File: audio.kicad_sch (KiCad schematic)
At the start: 8 parts, among them J1 1775443-2, U11 MAX98357AETE_T

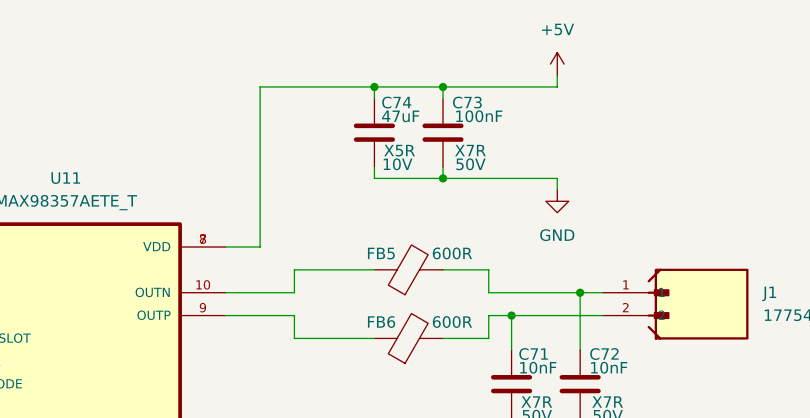
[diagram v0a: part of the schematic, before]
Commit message: modifications for manufacturing
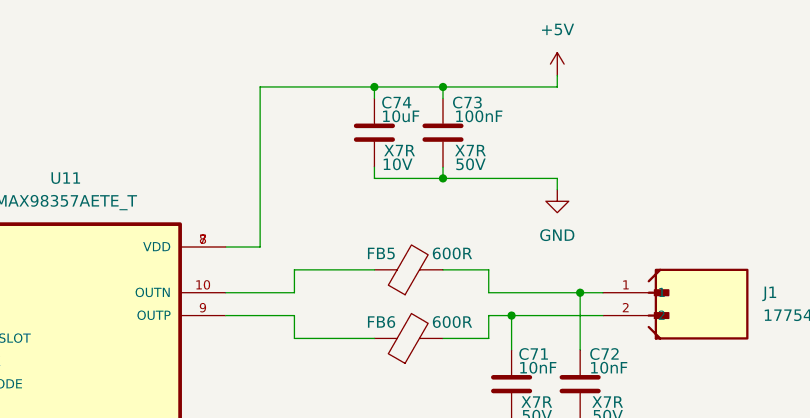
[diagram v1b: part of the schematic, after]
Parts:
- C73: Supplier Part (none) -> C49678
- C74: value 47uF -> 10uF; Dielectric X5R -> X7R; Supplier Part (none) -> C86038
- FB5, FB6: MANUFACTURER (none) -> Murata Electronics; MP (none) -> BLM18KG601SN1D; Part number BLM18AG601SN1D -> BLM18KG601SN1D; Supplier Part (none) -> C85833
- J1: Supplier Part (none) -> C5162845
- U11: Availability In Stock -> (none); Check_prices https://www.snapeda.com/parts/MAX98357AETE+T/Analog+Devices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 -> (none); Description_1 Tiny, Low-Cost, PCM Class D Amplifier with Class AB Perform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 -> (none); MANUFACTURER (none) -> Analog Devices Inc./Maxim Integrated; Package TQFN-16 Maxim -> TQFN-16-EP(3x3); Price None -> (none); Supplier Part (none) -> C910544
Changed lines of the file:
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@@
+			)
+		)
+		(property "Supplier Part" "C5162845"
+			(at 196.85 80.01 0)
+			(effects
+				(font
+					(size 1.27 1.27)
+				)
+				(hide yes)
 			)
 		)
@@
 			)
 		)
-		(property "Value" "47uF"
+		(property "Value" "10uF"
 			(at 167.132 60.452 0)
 			(effects
@@
 			)
 		)
-		(property "Dielectric" "X5R"
+		(property "Dielectric" "X7R"
 			(at 169.164 64.262 0)
 			(effects
@@
 		)
 		(property "Function" "AUDIO"
+			(at 166.37 62.23 0)
+			(effects
+				(font
+					(size 1.27 1.27)
+				)
+				(hide yes)
+			)
+		)
+		(property "Supplier Part" "C86038"
 			(at 166.37 62.23 0)
 			(effects
@@
 			)
 		)
-		(property "Part number" "BLM18AG601SN1D"
+		(property "Part number" "BLM18KG601SN1D"
 			(at 170.18 77.47 90)
 			(effects
@@
 		)
 		(property "Manufacturer" "Murata"
+			(at 170.18 77.47 90)
+			(effects
+				(font
+					(size 1.27 1.27)
+				)
+				(hide yes)
+			)
+		)
+		(property "Supplier Part" "C85833"
+			(at 170.18 77.47 90)
+			(effects
+				(font
+					(size 1.27 1.27)
+				)
+				(hide yes)
+			)
+		)
+		(property "MANUFACTURER" "Murata Electronics"
+			(at 170.18 77.47 90)
+			(effects
+				(font
+					(size 1.27 1.27)
+				)
+				(hide yes)
+			)
+		)
+		(property "MP" "BLM18KG601SN1D"
 			(at 170.18 77.47 90)
 			(effects
@@
 			)
 		)
+		(property "Supplier Part" "C49678"
+			(at 173.99 62.23 0)
+			(effects
+				(font
+					(size 1.27 1.27)
+				)
+				(hide yes)
+			)
+		)
 		(pin "1"
 		)
@@
 			)
 		)
-		(property "Part number" "BLM18AG601SN1D"
+		(property "Part number" "BLM18KG601SN1D"
 			(at 170.18 85.09 90)
 			(effects
@@
 		)
 		(property "Manufacturer" "Murata"
+			(at 170.18 85.09 90)
+			(effects
+				(font
+					(size 1.27 1.27)
+				)
+				(hide yes)
+			)
+		)
+		(property "Supplier Part" "C85833"
+			(at 170.18 85.09 90)
+			(effects
+				(font
+					(size 1.27 1.27)
+				)
+				(hide yes)
+			)
+		)
+		(property "MANUFACTURER" "Murata Electronics"
+			(at 170.18 85.09 90)
+			(effects
+				(font
+					(size 1.27 1.27)
+				)
+				(hide yes)
+			)
+		)
+		(property "MP" "BLM18KG601SN1D"
 			(at 170.18 85.09 90)
 			(effects
@@
 			)
 		)
-		(property "Description" ""
+		(property "Description" "Monaural 3.2Wx2@4Ω TQFN-16-EP(3x3) Audio Amplifiers ROHS"
 			(at 132.08 87.63 0)
 			(effects
@@
 			)
 		)
-		(property "Description_1" "Tiny, Low-Cost, PCM Class D Amplifier with Class AB Performance"
+		(property "Package" "TQFN-16-EP(3x3)"
 			(at 132.08 87.63 0)
 			(effects
@@
 			)
 		)
-		(property "Package" "TQFN-16 Maxim"
+		(property "SnapEDA_Link" "https://www.snapeda.com/parts/MAX98357AETE+T/Analog+Devices/view-part/?ref=snap"
 			(at 132.08 87.63 0)
 			(effects
@@
 			)
 		)
-		(property "Price" "None"
+		(property "MP" "MAX98357AETE+T"
 			(at 132.08 87.63 0)
 			(effects
@@
 			)
 		)
-		(property "SnapEDA_Link" "https://www.snapeda.com/parts/MAX98357AETE+T/Analog+Devices/view-part/?ref=snap"
-			(at 132.08 87.63 0)
-			(effects
-				(font
-					(size 1.27 1.27)
-				)
-				(justify bottom)
-				(hide yes)
-			)
-		)
-		(property "MP" "MAX98357AETE+T"
-			(at 132.08 87.63 0)
-			(effects
-				(font
-					(size 1.27 1.27)
-				)
-				(justify bottom)
-				(hide yes)
-			)
-		)
-		(property "Availability" "In Stock"
-			(at 132.08 87.63 0)
-			(effects
-				(font
-					(size 1.27 1.27)
-				)
-				(justify bottom)
-				(hide yes)
-			)
-		)
-		(property "Check_prices" "https://www.snapeda.com/parts/MAX98357AETE+T/Analog+Devices/view-part/?ref=eda"
-			(at 132.08 87.63 0)
-			(effects
-				(font
-					(size 1.27 1.27)
-				)
-				(justify bottom)
-				(hide yes)
-			)
-		)
 		(property "Function" "AUDIO"
 			(at 132.08 87.63 0)
 			(effects
+				(font
+					(size 1.27 1.27)
+				)
+				(hide yes)
+			)
+		)
+		(property "Supplier Part" "C910544"
+			(at 132.08 87.63 0)
+			(effects
+				(font
+					(size 1.27 1.27)
+				)
+				(hide yes)
+			)
+		)
+		(property "MANUFACTURER" "Analog Devices Inc./Maxim Integrated"
+			(at 132.08 87.63 0)
+			(effects

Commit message: modifications for manufacturing
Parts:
- C71, C72: Supplier Part (none) -> C1710
- FB5, FB6: Manufacturer Part (none) -> BLM18KG601SN1D
- J1: Manufacturer (none) -> TE Connectivity; Manufacturer Part (none) -> 1775443-2
- U11: Manufacturer (none) -> Analog Devices Inc./Maxim Integrated; Manufacturer Part (none) -> MAX98357AETE+T
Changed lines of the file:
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@@
+			)
+		)
+		(property "Manufacturer" "TE Connectivity"
+			(at 196.85 80.01 0)
+			(effects
+				(font
+					(size 1.27 1.27)
+				)
+				(hide yes)
+			)
+		)
+		(property "Manufacturer Part" "1775443-2"
+			(at 196.85 80.01 0)
+			(effects
+				(font
+					(size 1.27 1.27)
+				)
+				(hide yes)
 			)
 		)
@@
 		)
 		(property "MP" "BLM18KG601SN1D"
+			(at 170.18 77.47 90)
+			(effects
+				(font
+					(size 1.27 1.27)
+				)
+				(hide yes)
+			)
+		)
+		(property "Manufacturer Part" "BLM18KG601SN1D"
 			(at 170.18 77.47 90)
 			(effects
@@
 			)
 		)
+		(property "Supplier Part" "C1710"
+			(at 189.23 90.17 0)
+			(effects
+				(font
+					(size 1.27 1.27)
+				)
+				(hide yes)
+			)
+		)
 		(pin "1"
 		)
@@
 		)
 		(property "MP" "BLM18KG601SN1D"
+			(at 170.18 85.09 90)
+			(effects
+				(font
+					(size 1.27 1.27)
+				)
+				(hide yes)
+			)
+		)
+		(property "Manufacturer Part" "BLM18KG601SN1D"
 			(at 170.18 85.09 90)
 			(effects
@@
 			)
 		)
+		(property "Manufacturer" "Analog Devices Inc./Maxim Integrated"
+			(at 132.08 87.63 0)
+			(effects
+				(font
+					(size 1.27 1.27)
+				)
+				(hide yes)
+			)
+		)
+		(property "Manufacturer Part" "MAX98357AETE+T"
+			(at 132.08 87.63 0)
+			(effects
+				(font
+					(size 1.27 1.27)
+				)
+				(hide yes)
+			)
+		)
 		(pin "7"
 		)
@@
 			(at 181.61 90.17 0)
 			(effects
+				(font
+					(size 1.27 1.27)
+				)
+				(hide yes)
+			)
+		)
+		(property "Supplier Part" "C1710"
+			(at 181.61 90.17 0)
+			(effects

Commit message: modifications for manufacturing
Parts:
- C73: Manufacturer (none) -> YAGEO; Manufacturer Part (none) -> CC0805KRX7R9BB104
- C74: Manufacturer (none) -> Murata Electronics; Manufacturer Part (none) -> GRM21BR71A106KE51L
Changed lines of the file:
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@@
+			)
+		)
+		(property "Manufacturer" "Murata Electronics"
+			(at 166.37 62.23 0)
+			(effects
+				(font
+					(size 1.27 1.27)
+				)
+				(hide yes)
+			)
+		)
+		(property "Manufacturer Part" "GRM21BR71A106KE51L"
+			(at 166.37 62.23 0)
+			(effects
+				(font
+					(size 1.27 1.27)
+				)
+				(hide yes)
 			)
 		)
@@
 			(at 173.99 62.23 0)
 			(effects
+				(font
+					(size 1.27 1.27)
+				)
+				(hide yes)
+			)
+		)
+		(property "Manufacturer" "YAGEO"
+			(at 173.99 62.23 0)
+			(effects
+				(font
+					(size 1.27 1.27)
+				)
+				(hide yes)
+			)
+		)
+		(property "Manufacturer Part" "CC0805KRX7R9BB104"
+			(at 173.99 62.23 0)
+			(effects

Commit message: modifications for manufacturing
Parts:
- C71, C72: LCSC Part # (none) -> C1710
- C73: LCSC Part # (none) -> C49678
- C74: LCSC Part # (none) -> C86038
- FB5, FB6: LCSC Part # (none) -> C85833
- J1: LCSC Part # (none) -> C5162845
- U11: LCSC Part # (none) -> C910544
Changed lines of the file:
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@@
+			)
+		)
+		(property "LCSC Part #" "C5162845"
+			(at 196.85 80.01 0)
+			(effects
+				(font
+					(size 1.27 1.27)
+				)
+				(hide yes)
 			)
 		)
@@
 			)
 		)
+		(property "LCSC Part #" "C86038"
+			(at 166.37 62.23 0)
+			(effects
+				(font
+					(size 1.27 1.27)
+				)
+				(hide yes)
+			)
+		)
 		(pin "1"
 		)
@@
 		)
 		(property "Manufacturer Part" "BLM18KG601SN1D"
+			(at 170.18 77.47 90)
+			(effects
+				(font
+					(size 1.27 1.27)
+				)
+				(hide yes)
+			)
+		)
+		(property "LCSC Part #" "C85833"
 			(at 170.18 77.47 90)
 			(effects
@@
 			)
 		)
+		(property "LCSC Part #" "C49678"
+			(at 173.99 62.23 0)
+			(effects
+				(font
+					(size 1.27 1.27)
+				)
+				(hide yes)
+			)
+		)
 		(pin "1"
 		)
@@
 			)
 		)
+		(property "LCSC Part #" "C1710"
+			(at 189.23 90.17 0)
+			(effects
+				(font
+					(size 1.27 1.27)
+				)
+				(hide yes)
+			)
+		)
 		(pin "1"
 		)
@@
 		)
 		(property "Manufacturer Part" "BLM18KG601SN1D"
+			(at 170.18 85.09 90)
+			(effects
+				(font
+					(size 1.27 1.27)
+				)
+				(hide yes)
+			)
+		)
+		(property "LCSC Part #" "C85833"
 			(at 170.18 85.09 90)
 			(effects
@@
 			)
 		)
+		(property "LCSC Part #" "C910544"
+			(at 132.08 87.63 0)
+			(effects
+				(font
+					(size 1.27 1.27)
+				)
+				(hide yes)
+			)
+		)
 		(pin "7"
 		)
@@
 			(at 181.61 90.17 0)
 			(effects
+				(font
+					(size 1.27 1.27)
+				)
+				(hide yes)
+			)
+		)
+		(property "LCSC Part #" "C1710"
+			(at 181.61 90.17 0)
+			(effects

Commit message: complete redesign
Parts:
- removed C71, C72: 10nF, Capacitor_SMD:C_0805_2012Metric, symbol Device:C
- removed C73: 100nF, Capacitor_SMD:C_0805_2012Metric, symbol Device:C
- removed FB5, FB6: 600R, Onju:BLM18PG121SN1D, symbol Device:FerriteBead
- removed U11: MAX98357AETE_T, Onju:max98357aete, symbol New_Library:MAX98357AETE_T
- added C59, C60, C62, C86: 22uF, Capacitor_SMD:C_0805_2012Metric, symbol Device:C
- added C75, C76, C77: 0.22uF, Capacitor_SMD:C_0603_1608Metric, symbol Device:C
- added C78, C79: 0.68uF, Capacitor_SMD:C_0805_2012Metric, symbol Device:C
- added C87, C88: 100nF, Capacitor_SMD:C_0402_1005Metric, symbol Device:C
- added C89: 220uF, Capacitor_SMD:C_Elec_6.3x7.7, symbol Device:C_Polarized
- added C90: 4.7uF, Capacitor_SMD:C_0603_1608Metric, symbol Device:C
- added C91: 100nF, Capacitor_SMD:C_0603_1608Metric, symbol Device:C
- added L6, L7: 10uH, Onju:XAL4040-103MEC, symbol Device:L
- added R36, R38: 0R, Resistor_SMD:R_0805_2012Metric, symbol Seeed_libdb:Resistors/301010000
- added R39: 0R, Resistor_SMD:R_0603_1608Metric, symbol Device:R
- added R40: 0R, Resistor_SMD:R_0402_1005Metric, symbol Device:R
- added R67: 0R, Resistor_SMD:R_1206_3216Metric, symbol Device:R
- added R68: 47k, Resistor_SMD:R_0402_1005Metric, symbol Device:R
- added U12: TAS5805MPWPR, Onju:TAS5805MPWPR, symbol New_Library:TAS5805MPWPR
- C74: value 10uF -> 0.22uF; footprint Capacitor_SMD:C_0805_2012Metric -> Capacitor_SMD:C_0603_1608Metric; Function AUDIO -> TAS; LCSC Part # C86038 -> (none); Manufacturer Murata Electronics -> (none); Manufacturer Part GRM21BR71A106KE51L -> (none); Supplier Part C86038 -> (none); Voltage 10V -> 50V
- renumbered J1 to J5
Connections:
- net AUDIO_PA_EN: now also R68.2, U12.12 (~{PDN})
- net GND: now also R36.1, R38.1; no longer C74.2
- net I2S_BCLK: now also U12.7 (SCLK)
- net I2S_DIN_ESP: now also U12.8 (SDIN)
- net I2S_LRCK: now also U12.6 (LRCLK)
- net at J5.1: now also C78.1, L6.2
- net at J5.2: now also C79.1, L7.2
- net +5V: no longer names the net of C74.1
- net +5V: now also C75.1, L6.1, U12.17 (OUT_B+), U12.26 (OUT_A+)
- new net: C74.2, U12.25 (BST_A+)
- new net: R40.2, U12.3 (ADR/~{FAULT})
- new net: C75.2, U12.18 (BST_B+)
- new net: C76.1, C77.1, L7.1, U12.20 (OUT_B-), U12.23 (OUT_A-)
- new net: C76.2, U12.22 (BST_A-)
- new net: C77.2, U12.21 (BST_B-)
- new net +14V: R67.1
- new net +3V3: R39.1
- new net DGND: C59.2, C60.2, C62.2, C78.2, C79.2, C86.2, C87.2, C88.2, C89.2, C90.2, C91.2, R36.2, R38.2, R40.1, R68.1, U12.1 (DGND), U12.13 (AVDD), U12.14 (AGND), U12.19 (PGND), U12.24 (PGND), U12.29 (POWERPAD), U12.30 (POWERPAD), U12.31 (POWERPAD), U12.32 (POWERPAD), U12.33 (POWERPAD), U12.34 (POWERPAD), U12.35 (POWERPAD), U12.36 (POWERPAD), U12.37 (POWERPAD), U12.38 (POWERPAD), U12.39 (POWERPAD), U12.4 (VR_DIG), U12.40 (POWERPAD), U12.41 (POWERPAD), U12.42 (POWERPAD), U12.43 (POWERPAD), U12.44 (POWERPAD), U12.45 (POWERPAD), U12.46 (POWERPAD), U12.47 (POWERPAD), U12.48 (POWERPAD), U12.49 (POWERPAD), U12.5 (DGND), U12.50 (POWERPAD), U12.51 (POWERPAD), U12.52 (POWERPAD), U12.53 (POWERPAD)
- new net DVDD: C90.1, C91.1, R39.2, U12.2 (DVDD)
- new net I2C_SCL: U12.11 (SCL)
- new net I2C_SDA: U12.10 (SDA)
- new net PVDD: C59.1, C60.1, C62.1, C86.1, C87.1, C88.1, C89.1, R67.2, U12.15 (PVDD), U12.16 (PVDD), U12.27 (PVDD), U12.28 (PVDD)
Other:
- title: Nest mini drop in PCB replacement -> Drop in replacement PCB for Nest mini GEN2
- moved on the sheet: J5

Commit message: work in progress
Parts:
- added TP9: TestPoint, TestPoint:TestPoint_Pad_D1.0mm, symbol Connector:TestPoint
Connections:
- net AUDIO_PA_EN: now also TP9.1
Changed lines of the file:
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@@
+	)
+	(junction
+		(at 95.25 86.36)
+		(diameter 0)
+		(color 0 0 0 0)
 	)
 	(junction
@@
 	(wire
 		(pts
-			(xy 93.98 86.36) (xy 100.33 86.36)
+			(xy 93.98 86.36) (xy 95.25 86.36)
 		)
 		(stroke
@@
 	(wire
 		(pts
+			(xy 95.25 85.09) (xy 95.25 86.36)
+		)
+		(stroke
+			(width 0)
+			(type default)
+		)
+	)
+	(wire
+		(pts
 			(xy 88.9 99.06) (xy 149.86 99.06)
 		)
@@
 		(pts
 			(xy 109.22 104.14) (xy 111.76 104.14)
+		)
+		(stroke
+			(width 0)
+			(type default)
+		)
+	)
+	(wire
+		(pts
+			(xy 95.25 86.36) (xy 100.33 86.36)
 		)
 		(stroke
@@
 					(unit 1)
 				)
+			)
+		)
+	)
+	(symbol
+		(lib_id "Connector:TestPoint")
+		(at 95.25 85.09 0)
+		(unit 1)
+		(exclude_from_sim no)
+		(in_bom no)
+		(on_board yes)
+		(dnp yes)
+		(property "Reference" "TP9"
+			(at 93.726 79.502 0)
+			(effects
+				(font
+					(size 1.27 1.27)
+				)
+				(justify left)
+			)
+		)
+		(property "Value" "TestPoint"
+			(at 97.79 83.0579 0)
+			(effects
+				(font
+					(size 1.27 1.27)
+				)
+				(justify left)
+				(hide yes)
+			)
+		)
+		(property "Footprint" "TestPoint:TestPoint_Pad_D1.0mm"
+			(at 100.33 85.09 0)
+			(effects
+				(font
+					(size 1.27 1.27)
+				)
+				(hide yes)
+			)
+		)
+		(property "Datasheet" "~"
+			(at 100.33 85.09 0)
+			(effects
+				(font
+					(size 1.27 1.27)
+				)
+				(hide yes)
+			)
+		)
+		(property "Description" "test point"
+			(at 95.25 85.09 0)
+			(effects
+				(font
+					(size 1.27 1.27)
+				)
+				(hide yes)
+			)
+		)
+		(pin "1"
+		)
+		(instances
+			(project ""
+				(path "/204e071a-14ed-47a0-be54-332ac2b951cf/62ce711e-2967-4164-94ee-cdd918e5185e"
+					(reference "TP9")
+					(unit 1)
+				)

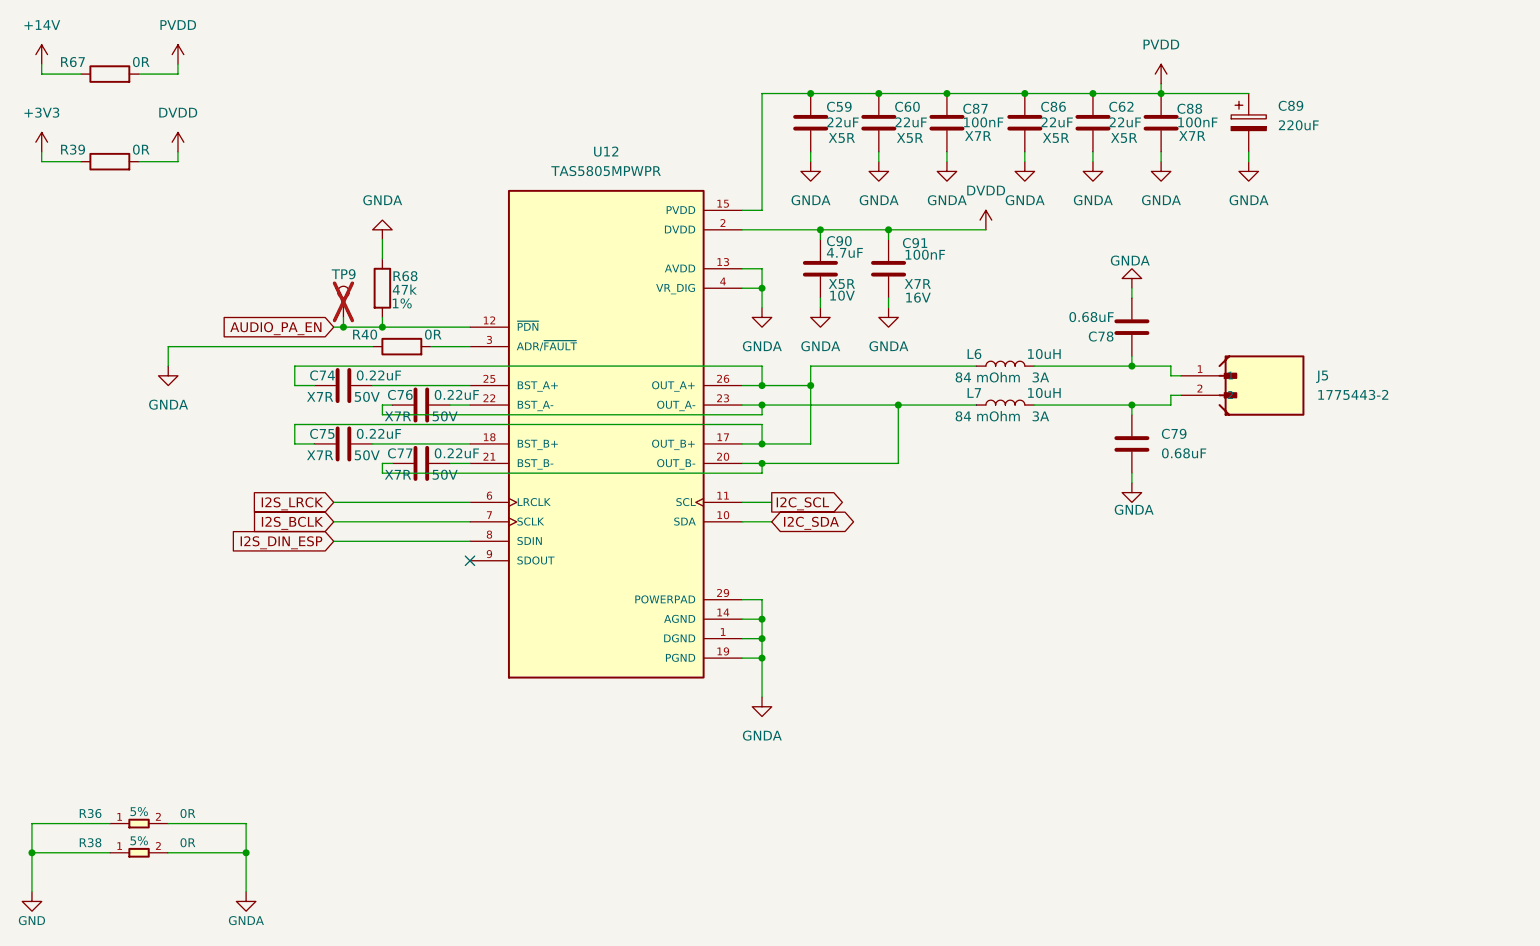
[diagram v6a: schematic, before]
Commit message: v2 hardware revision
MPR121 touch controller added to replace the esp32-s3 internal touch interface
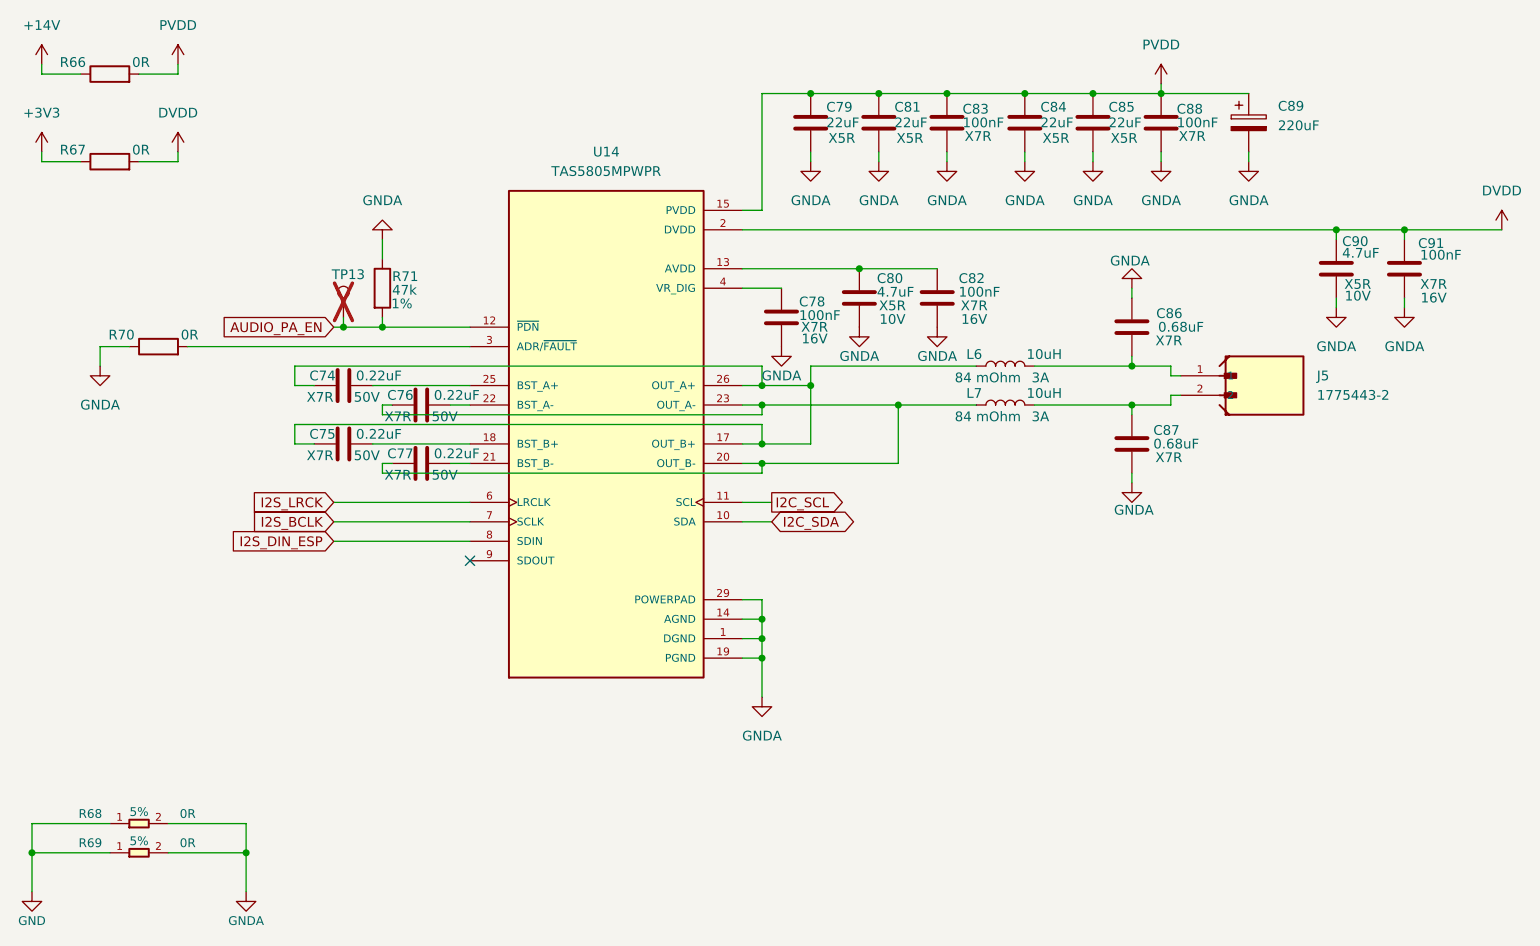
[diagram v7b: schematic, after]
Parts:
- added C78: 100nF, Capacitor_SMD:C_0402_1005Metric, symbol Device:C
- added C80: 4.7uF, Capacitor_SMD:C_0603_1608Metric, symbol Device:C
- added C82: 100nF, Capacitor_SMD:C_0603_1608Metric, symbol Device:C
- renumbered C59 to C79, C60 to C81, C87 to C83, C86 to C84, C62 to C85, C78 to C86, C79 to C87, R67 to R66, R39 to R67, R36 to R68, R38 to R69, R40 to R70, R68 to R71, TP9 to TP13, U12 to U14
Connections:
- net DGND: now also C78.2, C80.2, C82.2; no longer U14.13 (AVDD), U14.4 (VR_DIG)
- new net: C80.1, C82.1, U14.13 (AVDD)
- new net: C78.1, U14.4 (VR_DIG)
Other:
- moved on the sheet: C90, C91, R70
